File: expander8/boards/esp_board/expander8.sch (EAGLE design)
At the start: 63 parts, among them IC1 STM32F10XCXT6, IC2 78L05F, J1 DCJ0202

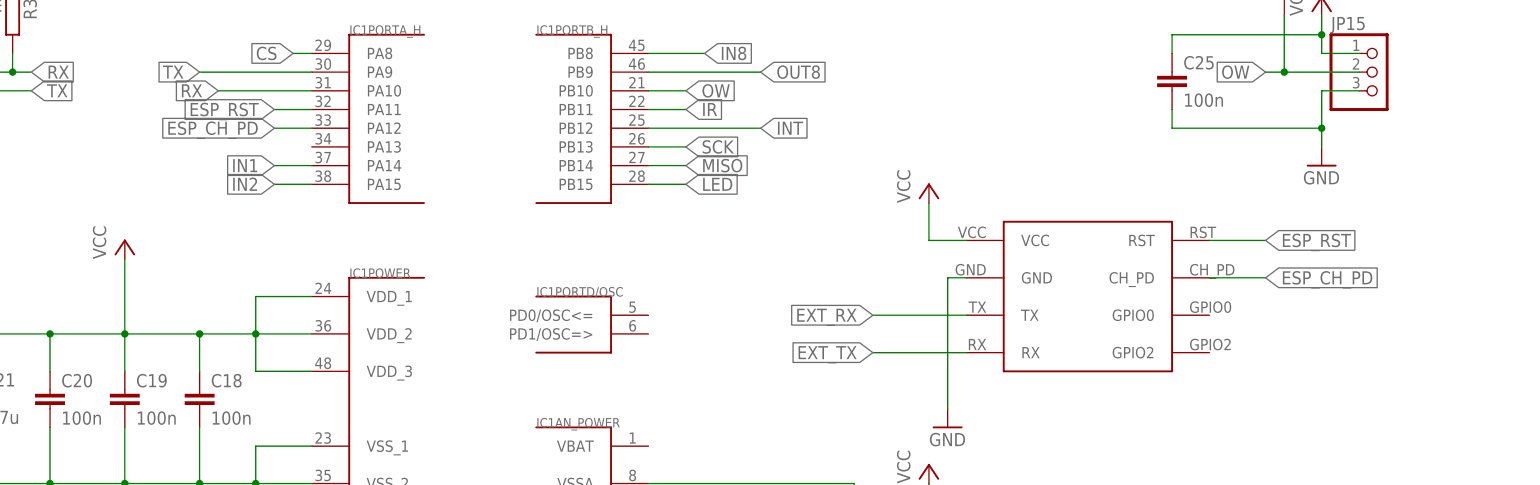
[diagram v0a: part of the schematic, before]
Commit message: added ESP GPIO2 connection
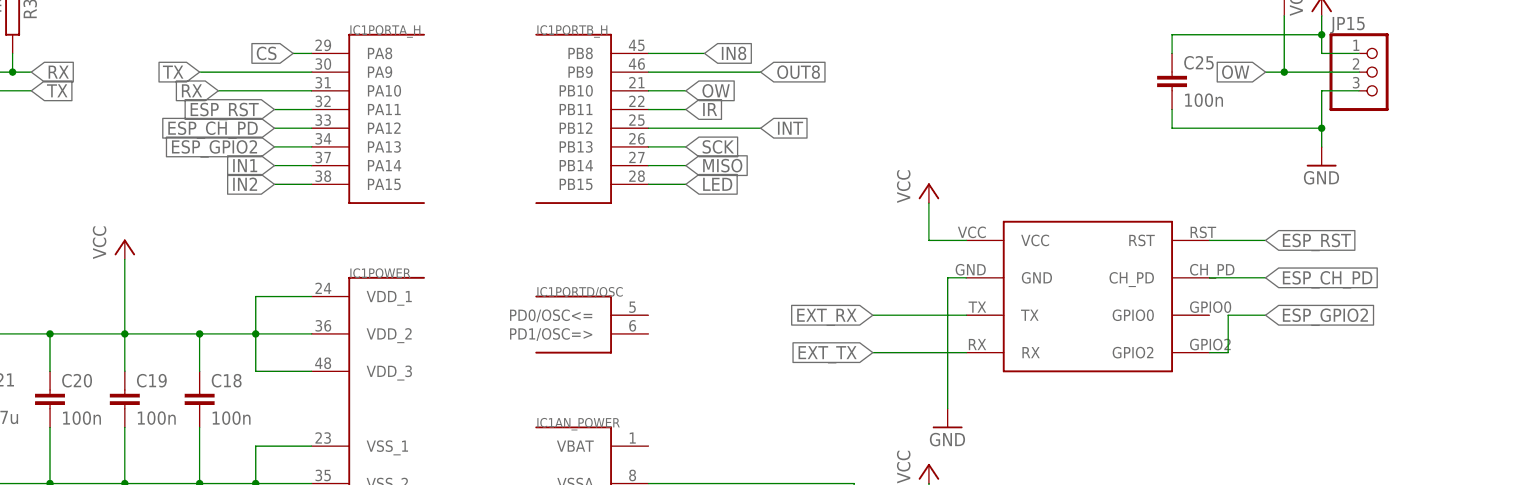
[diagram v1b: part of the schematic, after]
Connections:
- new net ESP_GPIO2: IC1PORTA_H.PA13, U$1.GPIO2
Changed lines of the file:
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@@
+</segment>
+</net>
+<net name="ESP_GPIO2" class="0">
+<segment>
+<pinref part="IC1" gate="PORTA_H" pin="PA13"/>
+<wire x1="-510.54" y1="142.24" x2="-515.62" y2="142.24" width="0.1524" layer="91"/>
+<label x="-515.62" y="142.24" size="1.778" layer="95" rot="R180" xref="yes"/>
+</segment>
+<segment>
+<label x="-381" y="119.38" size="1.778" layer="95" xref="yes"/>
+<pinref part="U$1" gate="G$1" pin="GPIO2"/>
+<wire x1="-386.08" y1="119.38" x2="-381" y2="119.38" width="0.1524" layer="91"/>
+<wire x1="-388.62" y1="114.3" x2="-386.08" y2="114.3" width="0.1524" layer="91"/>
+<wire x1="-386.08" y1="114.3" x2="-386.08" y2="119.38" width="0.1524" layer="91"/>
 </segment>
 </net>

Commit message: update
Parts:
- removed C24: 100n, rcl-kd:C-EUC0805
- removed F1: (no value), fuse:SHK20L
- removed PAD1, PAD2: (no value), wirepad:SMD2
- removed R21: 1M, rcl-kd:R-EU_R1206
- removed R24: 360, rcl:R-EU_M1206
- removed R27, R28, R29: 1, rcl-kd:R-EU_R1206
- removed R30: 4k7, resistor:R-EU_R0805
- removed U$6: MC33063/MC34063D, adafruit:MC33063/MC34063D
- added C11, C12, C13, C15, C16, C4, C5, C6, C7, C8, C9: 100n, rcl-kd:C-EUC0805
- added C3: 10n, rcl-kd:C-EUC1206
- added IC5: (no value), SparkFun:V_REG_LM1117SOT223
- added JP17: (no value), pinhead:PINHD-1X2_2.54
- added R10, R12, R13, R14, R15, R16, R17, R19, R22, R9: 0, resistor:R-EU_R0805
- added R11, R4, R5: 4k7, resistor:R-EU_R0805
- added R3: 0, rcl:R-EU_M1206
- added R35: (no value), resistor:R-EU_R1206
- added R36: (no value), resistor:R-EU_R0805
- added R8: 220, resistor:R-EU_R1206
- added S1: (no value), switch-omron:10-XX
- added U$2: USB-MINIB-5PIN, SparkFun:USB-MINIB-5PIN
- added U$3: FT230XQ, ftdi_ft231xq-r2:FT230XQ
- added U$4: DS1820TO92, Ava_ds18:DS1820TO92
- C10: value 220p -> 100n
- C30: device rcl-kd:C-EUC1206 -> rcl-kd:C-EUC0805
- C31: device rcl-kd:C-EUC0805 -> rcl-kd:C-EUC1206
- IC2: value 78L05F -> (none); device linear:78L05F -> lm2674:LM2674
- JP1: device pinhead-kd:PINHD-1X2 -> pinhead:PINHD-1X2_2.54
- JP3: device pinhead:PINHD-1X3 -> pinhead-kd:PINHD-1X2
- R2: value 0 -> 4k7; device resistor:R-EU_R0805 -> rcl-kd:R-EU_R0805
- R25: value 220 -> 4k7; device rcl:R-EU_M1206 -> resistor:R-EU_R0805
- R31: device resistor:R-EU_R0805 -> resistor:R-EU_R1206
- R34: device rcl-kd:R-EU_R1206 -> rcl-kd:R-EU_R0805
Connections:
- removed net COMP: R24.2, R25.1, U$6.COMP
- removed net CS: IC1PORTA_H.PA8
- removed net INT: IC1PORTB_H.PB12
- removed net IPK: R27.2, R28.2, R29.2, U$6.DC, U$6.IPK, U$6.SWC
- removed net MISO: IC1PORTB_H.PB14
- removed net N$51: D3.C, L1.1, U$6.SWE
- removed net N$56: C10.1, U$6.TC
- removed net N$57: C28.+, C29.1, F1.1A, J1.1
- removed net N$9: C2.1, IC2.VO, JP16.3, R2.2
- removed net SCK: IC1PORTB_H.PB13
- new net AN_LIGHT: IC1PORTA_L.PA4, R8.1
- new net AN_LIGHT2: C7.1, JP3.2, R25.2, R8.2
- new net BTN1: IC1PORTB_H.PB14, R2.2, S1.S
- new net ESP_GPIO0: IC1PORTA_H.PA11, U$1.GPIO0
- new net IN1_: C13.1, JP4.1, R12.1, RN1.9
- new net IN2_: C16.1, JP7.1, R13.1, RN1.8
- new net IN3_: C12.1, JP8.1, R14.1, RN1.7
- new net IN4_: C11.1, JP9.1, R15.1, RN1.6
- new net IN5_: C10.1, JP10.1, R16.1, RN1.5
- new net IN6_: C9.1, JP11.1, R17.1, R9.1
- new net IN7_: C8.1, JP12.1, R10.1, R19.1
- new net IN8_: C1.1, JP13.1, R11.1, R22.1
- new net N$1: C3.2, D3.C, IC2.VSW, L1.2
- new net N$12: R9.2, RN1.4
- new net N$14: R10.2, RN1.3
- new net N$15: R11.2, RN1.2
- new net N$2: IC2.FB, R4.1, R5.1
- new net N$38: R35.1, U$2.D-
- new net N$39: R35.2, U$3.USBDM
- new net N$40: R36.2, U$3.USBDP
- new net N$41: R36.1, U$2.D+
- new net N$6: C3.1, IC2.CB
- new net N$7: J1.1, R3.1
- new net VCC_5V: C2.1, C27.+, C4.1, C6.1, IC5.IN, JP1.1, JP1.2, JP16.3, L1.1, R20.1, R4.2
- new net VCC_USB: U$2.VBUS
- net ESP_RST: now also IC1PORTA_H.PA8; no longer IC1PORTA_H.PA11
- net GND: now also C11.2, C12.2, C13.2, C15.2, C16.2, C4.2, C5.2, C6.2, C7.2, C8.2, C9.2, IC5.ADJ, R25.1, R5.2, S1.P, U$2.GND, U$3.CBUS0, U$3.GND1, U$3.GND2, U$3.GND3, U$4.GND; no longer C24.2, IC2.GND@1, JP3.3, PAD2.P, R25.2, R30.1, U$6.GND
- net IN1: now also R12.2; no longer JP4.1, RN1.9
- net IN2: now also R13.2; no longer JP7.1, RN1.8
- net IN3: now also R14.2; no longer JP8.1, RN1.7
- net IN4: now also R15.2; no longer JP9.1, RN1.6
- net IN5: now also R16.2; no longer JP10.1, RN1.5
- net IN6: now also R17.2; no longer JP11.1, RN1.4
- net IN7: now also R19.2; no longer JP12.1, RN1.3
- net IN8: now also R22.2; no longer JP13.1, RN1.2
- net N$64: now also JP17.2; no longer JP1.2
- net OUT7: now also IC1PORTB_H.PB12; no longer IC1PORTA_L.PA4
- net OW: now also U$4.DQ
- net RST1: no longer PAD1.P
- net RX: now also U$3.TXD; no longer JP3.2, R30.2
- net TX: now also U$3.RXD; no longer JP3.1
- net VCC: now also C15.1, C5.1, IC5.OUT@1, JP17.1, JP3.1, U$3.3V3OUT, U$3.RESET#, U$3.VCC, U$3.VCCIO, U$4.VCC; no longer C24.1, C27.+, JP1.1, L1.2, R20.1, R24.1
- net VCC_12V: now also C28.+, C29.1, IC2.VIN, R3.2; no longer C1.1, F1.2A, IC2.VI, R27.1, R28.1, R29.1, U$6.VCC
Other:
- note added: "KEEP_AWAKE#"
- moved on the sheet: C1, C10, C27, D3, JP1, JP15, L1, R2, R25, RN1
